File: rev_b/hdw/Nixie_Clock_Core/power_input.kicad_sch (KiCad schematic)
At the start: 24 parts

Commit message: lots more PCB placement
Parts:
- added J?: +24V IN, Connectors:BARREL_JACK, symbol Connector:Barrel_Jack_Switch
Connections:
- net +24Vin: now also J?.1
- net GND: now also J?.2, J?.3
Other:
- moved on the sheet: TP?
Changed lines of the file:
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@@
   (junction (at 245.11 57.15) (diameter 0) (color 0 0 0 0)
+  )
+  (junction (at 39.37 81.28) (diameter 0) (color 0 0 0 0)
   )
   (junction (at 121.92 138.43) (diameter 0) (color 0 0 0 0)
@@
     (stroke (width 0) (type default))
   )
+  (wire (pts (xy 54.61 76.2) (xy 54.61 57.15))
+    (stroke (width 0) (type default))
+  )
   (wire (pts (xy 165.1 57.15) (xy 162.56 57.15))
     (stroke (width 0) (type default))
@@
     (stroke (width 0) (type default))
   )
+  (wire (pts (xy 39.37 81.28) (xy 36.83 81.28))
+    (stroke (width 0) (type default))
+  )
+  (wire (pts (xy 39.37 81.28) (xy 39.37 78.74))
+    (stroke (width 0) (type default))
+  )
   (wire (pts (xy 162.56 59.69) (xy 165.1 59.69))
     (stroke (width 0) (type default))
@@
     (stroke (width 0) (type default))
   )
+  (wire (pts (xy 39.37 83.82) (xy 39.37 81.28))
+    (stroke (width 0) (type default))
+  )
   (wire (pts (xy 101.6 97.79) (xy 101.6 93.98))
     (stroke (width 0) (type default))
@@
     (stroke (width 0) (type default))
   )
+  (wire (pts (xy 39.37 78.74) (xy 36.83 78.74))
+    (stroke (width 0) (type default))
+  )
   (wire (pts (xy 203.2 105.41) (xy 203.2 102.87))
     (stroke (width 0) (type default))
@@
   )
   (wire (pts (xy 203.2 135.89) (xy 203.2 138.43))
+    (stroke (width 0) (type default))
+  )
+  (wire (pts (xy 36.83 76.2) (xy 54.61 76.2))
     (stroke (width 0) (type default))
   )
@@
     )
   )
-  (symbol (lib_id "Custom_Library:TP") (at 39.37 78.74 0) (unit 1)
-    (in_bom yes) (on_board yes) (dnp no)
-    (property "Reference" "TP?" (at 39.37 74.93 0)
-      (effects (font (size 1.27 1.27)))
-    )
-    (property "Value" "TP" (at 39.37 74.93 0)
-      (effects (font (size 1.27 1.27)) hide)
-    )
-    (property "Footprint" "Connector_PinHeader_2.54mm:PinHeader_1x01_P2.54mm_Horizontal" (at 39.37 78.74 0)
+  (symbol (lib_id "Custom_Library:TP") (at 39.37 104.14 0) (unit 1)
+    (in_bom yes) (on_board yes) (dnp no)
+    (property "Reference" "TP?" (at 39.37 100.33 0)
+      (effects (font (size 1.27 1.27)))
+    )
+    (property "Value" "TP" (at 39.37 100.33 0)
+      (effects (font (size 1.27 1.27)) hide)
+    )
+    (property "Footprint" "Connector_PinHeader_2.54mm:PinHeader_1x01_P2.54mm_Horizontal" (at 39.37 104.14 0)
       (effects (font (size 1.524 1.524)) hide)
     )
-    (property "Datasheet" "" (at 39.37 78.74 0)
+    (property "Datasheet" "" (at 39.37 104.14 0)
       (effects (font (size 1.524 1.524)))
     )
-    (property "Digi-Key PN" "" (at 39.37 78.74 0)
+    (property "Digi-Key PN" "" (at 39.37 104.14 0)
       (effects (font (size 1.27 1.27)) hide)
     )
@@
     )
   )
+  (symbol (lib_id "Connector:Barrel_Jack_Switch") (at 29.21 78.74 0) (unit 1)
+    (in_bom yes) (on_board yes) (dnp no)
+    (property "Reference" "J?" (at 29.21 73.406 0)
+      (effects (font (size 1.27 1.27)))
+    )
+    (property "Value" "+24V IN" (at 29.21 83.82 0)
+      (effects (font (size 1.27 1.27)))
+    )
+    (property "Footprint" "Connectors:BARREL_JACK" (at 30.48 79.756 0)
+      (effects (font (size 1.27 1.27)) hide)
+    )
+    (property "Datasheet" "~" (at 30.48 79.756 0)
+      (effects (font (size 1.27 1.27)) hide)
+    )
+    (property "Configuration" "DNP" (at 29.21 86.36 0)
+      (effects (font (size 1.27 1.27)))
+    )
+    (pin "1")
+    (pin "2")
+    (pin "3")
+    (instances
+      (project "Nixie_Clock_Core"
+        (path "/16fdce21-b570-4d81-a458-e8839d611806/0b6dccc1-0a92-424d-9916-2441ea7dc052"
+          (reference "J?") (unit 1)
+        )
+        (path "/16fdce21-b570-4d81-a458-e8839d611806/033277b9-3b61-4d88-889d-97b223ca74c5"
+          (reference "J202") (unit 1)
+        )
+      )
+      (project "LED_Panel_Controller"
+        (path "/22e05ee1-b227-4be7-9418-94433f274720/00000000-0000-0000-0000-00005f581b41"
+          (reference "J?") (unit 1)
+        )
+      )
+    )
+  )
   (symbol (lib_id "Custom_Library:C_Custom") (at 147.32 154.94 0) (unit 1)
     (in_bom yes) (on_board yes) (dnp no)
@@
     )
   )
-  (symbol (lib_id "power:GND") (at 39.37 78.74 0) (unit 1)
-    (in_bom yes) (on_board yes) (dnp no)
-    (property "Reference" "#PWR?" (at 39.37 85.09 0)
-      (effects (font (size 1.27 1.27)) hide)
-    )
-    (property "Value" "GND" (at 39.37 82.55 0)
-      (effects (font (size 1.27 1.27)))
-    )
-    (property "Footprint" "" (at 39.37 78.74 0)
-      (effects (font (size 1.27 1.27)) hide)
-    )
-    (property "Datasheet" "" (at 39.37 78.74 0)
+  (symbol (lib_id "power:GND") (at 39.37 104.14 0) (unit 1)
+    (in_bom yes) (on_board yes) (dnp no)
+    (property "Reference" "#PWR?" (at 39.37 110.49 0)
+      (effects (font (size 1.27 1.27)) hide)
+    )
+    (property "Value" "GND" (at 39.37 107.95 0)
+      (effects (font (size 1.27 1.27)))
+    )
+    (property "Footprint" "" (at 39.37 104.14 0)
+      (effects (font (size 1.27 1.27)) hide)
+    )
+    (property "Datasheet" "" (at 39.37 104.14 0)
       (effects (font (size 1.27 1.27)) hide)
     )
@@
     )
   )
-  (symbol (lib_id "power:GND") (at 26.67 78.74 0) (unit 1)
-    (in_bom yes) (on_board yes) (dnp no)
-    (property "Reference" "#PWR?" (at 26.67 85.09 0)
-      (effects (font (size 1.27 1.27)) hide)
-    )
-    (property "Value" "GND" (at 26.67 82.55 0)
-      (effects (font (size 1.27 1.27)))
-    )
-    (property "Footprint" "" (at 26.67 78.74 0)
-      (effects (font (size 1.27 1.27)) hide)
-    )
-    (property "Datasheet" "" (at 26.67 78.74 0)
+  (symbol (lib_id "power:GND") (at 26.67 104.14 0) (unit 1)
+    (in_bom yes) (on_board yes) (dnp no)
+    (property "Reference" "#PWR?" (at 26.67 110.49 0)
+      (effects (font (size 1.27 1.27)) hide)
+    )
+    (property "Value" "GND" (at 26.67 107.95 0)
+      (effects (font (size 1.27 1.27)))
+    )
+    (property "Footprint" "" (at 26.67 104.14 0)
+      (effects (font (size 1.27 1.27)) hide)
+    )
+    (property "Datasheet" "" (at 26.67 104.14 0)
       (effects (font (size 1.27 1.27)) hide)
     )
@@
     )
   )
-  (symbol (lib_id "power:PWR_FLAG") (at 26.67 78.74 0) (unit 1)
-    (in_bom yes) (on_board yes) (dnp no)
-    (property "Reference" "#FLG?" (at 26.67 76.835 0)
-      (effects (font (size 1.27 1.27)) hide)
-    )
-    (property "Value" "PWR_FLAG" (at 26.67 74.93 0)
-      (effects (font (size 1.27 1.27)))
-    )
-    (property "Footprint" "" (at 26.67 78.74 0)
-      (effects (font (size 1.27 1.27)) hide)
-    )
-    (property "Datasheet" "~" (at 26.67 78.74 0)
+  (symbol (lib_id "power:PWR_FLAG") (at 26.67 104.14 0) (unit 1)
+    (in_bom yes) (on_board yes) (dnp no)
+    (property "Reference" "#FLG?" (at 26.67 102.235 0)
+      (effects (font (size 1.27 1.27)) hide)
+    )
+    (property "Value" "PWR_FLAG" (at 26.67 100.33 0)
+      (effects (font (size 1.27 1.27)))
+    )
+    (property "Footprint" "" (at 26.67 104.14 0)
+      (effects (font (size 1.27 1.27)) hide)
+    )
+    (property "Datasheet" "~" (at 26.67 104.14 0)
       (effects (font (size 1.27 1.27)) hide)
     )
@@
         )
       )
+    )
+  )
+  (symbol (lib_id "power:GND") (at 39.37 83.82 0) (unit 1)
+    (in_bom yes) (on_board yes) (dnp no)
+    (property "Reference" "#PWR?" (at 39.37 90.17 0)
+      (effects (font (size 1.27 1.27)) hide)
+    )
+    (property "Value" "GND" (at 39.37 87.63 0)
+      (effects (font (size 1.27 1.27)))
+    )
+    (property "Footprint" "" (at 39.37 83.82 0)
+      (effects (font (size 1.27 1.27)) hide)
+    )
+    (property "Datasheet" "" (at 39.37 83.82 0)
+      (effects (font (size 1.27 1.27)) hide)
+    )
+    (pin "1")
+    (instances
+      (project "Nixie_Clock_Core"
+        (path "/16fdce21-b570-4d81-a458-e8839d611806/0b6dccc1-0a92-424d-9916-2441ea7dc052"
+          (reference "#PWR?") (unit 1)
+        )
+        (path "/16fdce21-b570-4d81-a458-e8839d611806/033277b9-3b61-4d88-889d-97b223ca74c5"
+          (reference "#PWR0208") (unit 1)
+        )
+      )
+      (project "LED_Panel_Controller"
+        (path "/22e05ee1-b227-4be7-9418-94433f274720/00000000-0000-0000-0000-00005f581b41"
+          (reference "#PWR?") (unit 1)
+        )
+      )

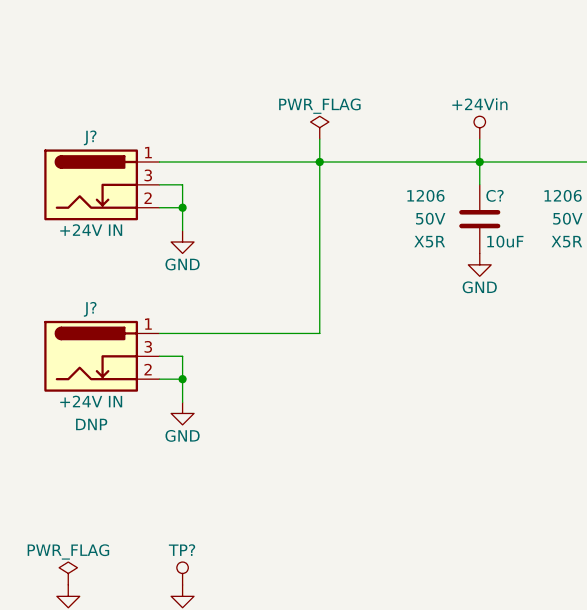
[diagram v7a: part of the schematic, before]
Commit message: started PCB design rules, some layout
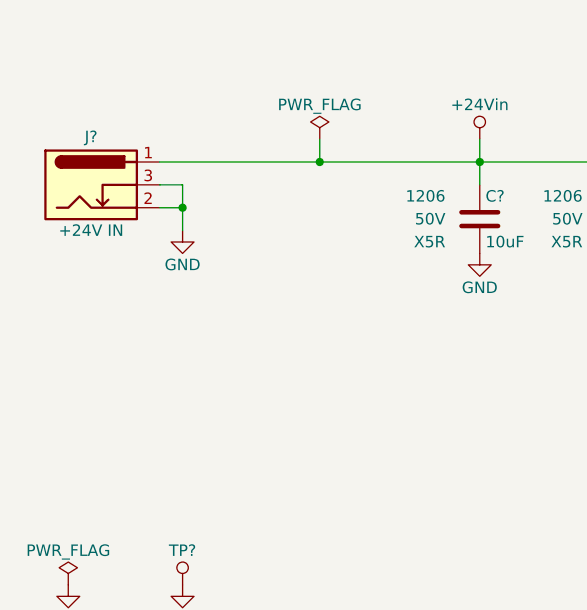
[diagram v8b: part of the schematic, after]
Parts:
- removed J?: +24V IN, Connectors:BARREL_JACK, symbol Connector:Barrel_Jack_Switch
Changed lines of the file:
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@@
   (junction (at 245.11 57.15) (diameter 0) (color 0 0 0 0)
-  )
-  (junction (at 39.37 81.28) (diameter 0) (color 0 0 0 0)
   )
   (junction (at 121.92 138.43) (diameter 0) (color 0 0 0 0)
@@
     (stroke (width 0) (type default))
   )
-  (wire (pts (xy 54.61 76.2) (xy 54.61 57.15))
-    (stroke (width 0) (type default))
-  )
   (wire (pts (xy 165.1 57.15) (xy 162.56 57.15))
     (stroke (width 0) (type default))
@@
     (stroke (width 0) (type default))
   )
-  (wire (pts (xy 39.37 81.28) (xy 36.83 81.28))
-    (stroke (width 0) (type default))
-  )
-  (wire (pts (xy 39.37 81.28) (xy 39.37 78.74))
-    (stroke (width 0) (type default))
-  )
   (wire (pts (xy 162.56 59.69) (xy 165.1 59.69))
     (stroke (width 0) (type default))
@@
     (stroke (width 0) (type default))
   )
-  (wire (pts (xy 39.37 83.82) (xy 39.37 81.28))
-    (stroke (width 0) (type default))
-  )
   (wire (pts (xy 101.6 97.79) (xy 101.6 93.98))
     (stroke (width 0) (type default))
@@
     (stroke (width 0) (type default))
   )
-  (wire (pts (xy 39.37 78.74) (xy 36.83 78.74))
-    (stroke (width 0) (type default))
-  )
   (wire (pts (xy 203.2 105.41) (xy 203.2 102.87))
     (stroke (width 0) (type default))
@@
   )
   (wire (pts (xy 203.2 135.89) (xy 203.2 138.43))
-    (stroke (width 0) (type default))
-  )
-  (wire (pts (xy 36.83 76.2) (xy 54.61 76.2))
     (stroke (width 0) (type default))
   )
@@
         (path "/22e05ee1-b227-4be7-9418-94433f274720/00000000-0000-0000-0000-00005eae2d66"
           (reference "R?") (unit 1)
-        )
-      )
-    )
-  )
-  (symbol (lib_id "Connector:Barrel_Jack_Switch") (at 29.21 78.74 0) (unit 1)
-    (in_bom yes) (on_board yes) (dnp no)
-    (property "Reference" "J?" (at 29.21 73.406 0)
-      (effects (font (size 1.27 1.27)))
-    )
-    (property "Value" "+24V IN" (at 29.21 83.82 0)
-      (effects (font (size 1.27 1.27)))
-    )
-    (property "Footprint" "Connectors:BARREL_JACK" (at 30.48 79.756 0)
-      (effects (font (size 1.27 1.27)) hide)
-    )
-    (property "Datasheet" "~" (at 30.48 79.756 0)
-      (effects (font (size 1.27 1.27)) hide)
-    )
-    (property "Configuration" "DNP" (at 29.21 86.36 0)
-      (effects (font (size 1.27 1.27)))
-    )
-    (pin "1")
-    (pin "2")
-    (pin "3")
-    (instances
-      (project "Nixie_Clock_Core"
-        (path "/16fdce21-b570-4d81-a458-e8839d611806/0b6dccc1-0a92-424d-9916-2441ea7dc052"
-          (reference "J?") (unit 1)
-        )
-        (path "/16fdce21-b570-4d81-a458-e8839d611806/033277b9-3b61-4d88-889d-97b223ca74c5"
-          (reference "J202") (unit 1)
-        )
-      )
-      (project "LED_Panel_Controller"
-        (path "/22e05ee1-b227-4be7-9418-94433f274720/00000000-0000-0000-0000-00005f581b41"
-          (reference "J?") (unit 1)
         )
       )
@@
         )
       )
-    )
-  )
-  (symbol (lib_id "power:GND") (at 39.37 83.82 0) (unit 1)
-    (in_bom yes) (on_board yes) (dnp no)
-    (property "Reference" "#PWR?" (at 39.37 90.17 0)
-      (effects (font (size 1.27 1.27)) hide)
-    )
-    (property "Value" "GND" (at 39.37 87.63 0)
-      (effects (font (size 1.27 1.27)))
-    )
-    (property "Footprint" "" (at 39.37 83.82 0)
-      (effects (font (size 1.27 1.27)) hide)
-    )
-    (property "Datasheet" "" (at 39.37 83.82 0)
-      (effects (font (size 1.27 1.27)) hide)
-    )
-    (pin "1")
-    (instances
-      (project "Nixie_Clock_Core"
-        (path "/16fdce21-b570-4d81-a458-e8839d611806/0b6dccc1-0a92-424d-9916-2441ea7dc052"
-          (reference "#PWR?") (unit 1)
-        )
-        (path "/16fdce21-b570-4d81-a458-e8839d611806/033277b9-3b61-4d88-889d-97b223ca74c5"
-          (reference "#PWR0208") (unit 1)
-        )
-      )
-      (project "LED_Panel_Controller"
-        (path "/22e05ee1-b227-4be7-9418-94433f274720/00000000-0000-0000-0000-00005f581b41"
-          (reference "#PWR?") (unit 1)
-        )
-      )
